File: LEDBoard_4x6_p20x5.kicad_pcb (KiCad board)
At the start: 2 copper layers, 0 parts

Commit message: fixed schematic ordering + placed parts
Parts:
- added C1: 10uF 6.3V, Capacitor_SMD:C_0603_1608Metric_Pad1.05x0.95mm_HandSolder, F.Cu at (75.2, 88.2)
- added C10: 100n, Capacitor_SMD:C_0603_1608Metric_Pad1.05x0.95mm_HandSolder, F.Cu at (122.2, 87.2)
- added C11: 10uF 6.3V, Capacitor_SMD:C_0603_1608Metric_Pad1.05x0.95mm_HandSolder, F.Cu at (115.2, 106.7)
- added C12: 100n, Capacitor_SMD:C_0603_1608Metric_Pad1.05x0.95mm_HandSolder, F.Cu at (122.2, 105.7)
- added C2: 100n, Capacitor_SMD:C_0603_1608Metric_Pad1.05x0.95mm_HandSolder, F.Cu at (82.2, 87.2)
- added C3: 10uF 6.3V, Capacitor_SMD:C_0603_1608Metric_Pad1.05x0.95mm_HandSolder, F.Cu at (75.2, 106.8)
- added C4: 100n, Capacitor_SMD:C_0603_1608Metric_Pad1.05x0.95mm_HandSolder, F.Cu at (82.2, 105.8)
- added C5: 10uF 6.3V, Capacitor_SMD:C_0603_1608Metric_Pad1.05x0.95mm_HandSolder, F.Cu at (115.2, 97.5)
- added C6: 100n, Capacitor_SMD:C_0603_1608Metric_Pad1.05x0.95mm_HandSolder, F.Cu at (122.2, 96.5)
- added C7: 10uF 6.3V, Capacitor_SMD:C_0603_1608Metric_Pad1.05x0.95mm_HandSolder, F.Cu at (75.2, 97.8)
- added C8: 100n, Capacitor_SMD:C_0603_1608Metric_Pad1.05x0.95mm_HandSolder, F.Cu at (82.2, 96.8)
- added C9: 10uF 6.3V, Capacitor_SMD:C_0603_1608Metric_Pad1.05x0.95mm_HandSolder, F.Cu at (115.2, 88.2)
- added D_0x0: LED_RGB, LEDs_SMD_NICHIA:LED_RGB_0706_1816Metric_ROHM_ThermalVias, F.Cu at (70.0, 87.5)
- added D_0x1: LED_RGB, LEDs_SMD_NICHIA:LED_RGB_0706_1816Metric_ROHM_ThermalVias, F.Cu at (70.0, 92.5)
- added D_0x2: LED_RGB, LEDs_SMD_NICHIA:LED_RGB_0706_1816Metric_ROHM_ThermalVias, F.Cu at (70.0, 97.5)
- added D_0x3: LED_RGB, LEDs_SMD_NICHIA:LED_RGB_0706_1816Metric_ROHM_ThermalVias, F.Cu at (70.0, 102.5)
- added D_0x4: LED_RGB, LEDs_SMD_NICHIA:LED_RGB_0706_1816Metric_ROHM_ThermalVias, F.Cu at (70.0, 107.5)
- added D_0x5: LED_RGB, LEDs_SMD_NICHIA:LED_RGB_0706_1816Metric_ROHM_ThermalVias, F.Cu at (70.0, 112.5)
- added D_1x0: LED_RGB, LEDs_SMD_NICHIA:LED_RGB_0706_1816Metric_ROHM_ThermalVias, F.Cu at (90.0, 87.5)
- added D_1x1: LED_RGB, LEDs_SMD_NICHIA:LED_RGB_0706_1816Metric_ROHM_ThermalVias, F.Cu at (90.0, 92.5)
- added D_1x2: LED_RGB, LEDs_SMD_NICHIA:LED_RGB_0706_1816Metric_ROHM_ThermalVias, F.Cu at (90.0, 97.5)
- added D_1x3: LED_RGB, LEDs_SMD_NICHIA:LED_RGB_0706_1816Metric_ROHM_ThermalVias, F.Cu at (90.0, 102.6)
- added D_1x4: LED_RGB, LEDs_SMD_NICHIA:LED_RGB_0706_1816Metric_ROHM_ThermalVias, F.Cu at (90.0, 107.5)
- added D_1x5: LED_RGB, LEDs_SMD_NICHIA:LED_RGB_0706_1816Metric_ROHM_ThermalVias, F.Cu at (90.0, 112.5)
- added D_2x0: LED_RGB, LEDs_SMD_NICHIA:LED_RGB_0706_1816Metric_ROHM_ThermalVias, F.Cu at (110.0, 87.5)
- added D_2x1: LED_RGB, LEDs_SMD_NICHIA:LED_RGB_0706_1816Metric_ROHM_ThermalVias, F.Cu at (110.0, 92.5)
- added D_2x2: LED_RGB, LEDs_SMD_NICHIA:LED_RGB_0706_1816Metric_ROHM_ThermalVias, F.Cu at (110.0, 97.5)
- added D_2x3: LED_RGB, LEDs_SMD_NICHIA:LED_RGB_0706_1816Metric_ROHM_ThermalVias, F.Cu at (110.0, 102.5)
- added D_2x4: LED_RGB, LEDs_SMD_NICHIA:LED_RGB_0706_1816Metric_ROHM_ThermalVias, F.Cu at (110.0, 107.5)
- added D_2x5: LED_RGB, LEDs_SMD_NICHIA:LED_RGB_0706_1816Metric_ROHM_ThermalVias, F.Cu at (110.0, 112.5)
- added D_3x0: LED_RGB, LEDs_SMD_NICHIA:LED_RGB_0706_1816Metric_ROHM_ThermalVias, F.Cu at (130.0, 87.5)
- added D_3x1: LED_RGB, LEDs_SMD_NICHIA:LED_RGB_0706_1816Metric_ROHM_ThermalVias, F.Cu at (130.0, 92.5)
- added D_3x2: LED_RGB, LEDs_SMD_NICHIA:LED_RGB_0706_1816Metric_ROHM_ThermalVias, F.Cu at (130.0, 97.5)
- added D_3x3: LED_RGB, LEDs_SMD_NICHIA:LED_RGB_0706_1816Metric_ROHM_ThermalVias, F.Cu at (130.0, 102.5)
- added D_3x4: LED_RGB, LEDs_SMD_NICHIA:LED_RGB_0706_1816Metric_ROHM_ThermalVias, F.Cu at (130.0, 107.5)
- added D_3x5: LED_RGB, LEDs_SMD_NICHIA:LED_RGB_0706_1816Metric_ROHM_ThermalVias, F.Cu at (130.0, 112.5)
- added H1: MH_M3, MountingHole:MountingHole_3.2mm_M3_ISO7380_Pad, F.Cu at (94.9, 95.0)
- added H2: MH_M3, MountingHole:MountingHole_3.2mm_M3_ISO7380_Pad, F.Cu at (105.0, 105.0)
- added J1: signal_in, Connector_PinHeader_2.54mm:PinHeader_1x04_P2.54mm_Vertical, F.Cu at (96.2, 88.5)
- added J2: signal_out, Connector_PinHeader_2.54mm:PinHeader_1x04_P2.54mm_Vertical, F.Cu at (96.2, 111.5)
- added J3: power_in, Connector_PinHeader_2.54mm:PinHeader_1x02_P2.54mm_Vertical, F.Cu at (96.2, 107.6)
- added J4: power_out, Connector_PinHeader_2.54mm:PinHeader_1x02_P2.54mm_Vertical, F.Cu at (101.3, 93.7)
- added R1: 2k7 0.1%, Resistor_SMD:R_0603_1608Metric_Pad1.05x0.95mm_HandSolder, F.Cu at (77.8, 87.2)
- added R2: 2k7 0.1%, Resistor_SMD:R_0603_1608Metric_Pad1.05x0.95mm_HandSolder, F.Cu at (77.8, 96.8)
- added R3: 2k7 0.1%, Resistor_SMD:R_0603_1608Metric_Pad1.05x0.95mm_HandSolder, F.Cu at (77.8, 105.8)
- added R4: 2k7 0.1%, Resistor_SMD:R_0603_1608Metric_Pad1.05x0.95mm_HandSolder, F.Cu at (117.8, 87.2)
- added R5: 2k7 0.1%, Resistor_SMD:R_0603_1608Metric_Pad1.05x0.95mm_HandSolder, F.Cu at (117.8, 96.5)
- added R6: 2k7 0.1%, Resistor_SMD:R_0603_1608Metric_Pad1.05x0.95mm_HandSolder, F.Cu at (117.8, 105.7)
- added U1: TLC5971PWP, Package_SO:HTSSOP-20-1EP_4.4x6.5mm_P0.65mm_EP3.4x6.5mm_Mask2.75x3.43mm_ThermalVias, F.Cu at (80.0, 91.5)
- added U2: TLC5971PWP, Package_SO:HTSSOP-20-1EP_4.4x6.5mm_P0.65mm_EP3.4x6.5mm_Mask2.75x3.43mm_ThermalVias, F.Cu at (80.0, 101.0)
- added U3: TLC5971PWP, Package_SO:HTSSOP-20-1EP_4.4x6.5mm_P0.65mm_EP3.4x6.5mm_Mask2.75x3.43mm_ThermalVias, F.Cu at (80.0, 110.0)
- added U4: TLC5971PWP, Package_SO:HTSSOP-20-1EP_4.4x6.5mm_P0.65mm_EP3.4x6.5mm_Mask2.75x3.43mm_ThermalVias, F.Cu at (120.0, 91.5)
- added U5: TLC5971PWP, Package_SO:HTSSOP-20-1EP_4.4x6.5mm_P0.65mm_EP3.4x6.5mm_Mask2.75x3.43mm_ThermalVias, F.Cu at (120.0, 101.0)
- added U6: TLC5971PWP, Package_SO:HTSSOP-20-1EP_4.4x6.5mm_P0.65mm_EP3.4x6.5mm_Mask2.75x3.43mm_ThermalVias, F.Cu at (120.0, 110.0)
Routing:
- added copper zone on B.Cu, net GND
- added copper zone on F.Cu, net VCC_LED
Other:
- board outline added: 64 x 28 mm

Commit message: pcb mostly done
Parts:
- moved C5 13.1 mm to (126.8, 103.8), turned to 180 degrees
- moved C9 13.1 mm to (126.8, 94.2), turned to 180 degrees
- moved C11 13.0 mm to (126.8, 112.8), turned to 180 degrees
- moved J1 9.00 mm to (96.2, 97.5)
- moved J2 9.00 mm to (96.2, 102.5)
- moved C3 6.56 mm to (73.2, 113.0), turned to 0 degrees
- moved C7 5.85 mm to (73.2, 103.2), turned to 0 degrees
- moved C1 5.43 mm to (73.2, 93.2), turned to 0 degrees
- moved H1 5.00 mm to (95.0, 90.0)
- moved H2 5.00 mm to (105.0, 110.0)
- moved C6 3.93 mm to (125.8, 98.2), turned to 0 degrees
- moved C10 3.82 mm to (125.8, 88.8), turned to 0 degrees
- moved C12 3.82 mm to (125.8, 107.2), turned to 0 degrees
- moved R5 3.82 mm to (114.2, 98.0), turned to 180 degrees
- moved R4 3.77 mm to (114.2, 88.4), turned to 180 degrees
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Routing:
- net VCC_LED: track 0.00 -> 494.7 mm
- net GND: track 0.00 -> 399.0 mm, vias 0 -> 29
- net VCC: track 0.00 -> 108.0 mm, vias 0 -> 12
- net /clock_3-4: track 0.00 -> 49.3 mm, vias 0 -> 4
- net /data_3-4: track 0.00 -> 48.6 mm, vias 0 -> 4
- net /data_out: track 0.00 -> 38.2 mm, vias 0 -> 1
- net /clock_out: track 0.00 -> 35.6 mm, vias 0 -> 1
- net /clock_in: track 0.00 -> 27.1 mm, vias 0 -> 2
- net /data_in: track 0.00 -> 22.9 mm, vias 0 -> 2
- net /clock_2-3: track 0.00 -> 21.6 mm, vias 0 -> 2
- net /data_2-3: track 0.00 -> 20.9 mm, vias 0 -> 2
- net /clock_4-5: track 0.00 -> 20.5 mm, vias 0 -> 2
- net /data_4-5: track 0.00 -> 20.2 mm, vias 0 -> 2
- net /clock_5-6: track 0.00 -> 19.8 mm, vias 0 -> 2
- net /data_5-6: track 0.00 -> 19.3 mm, vias 0 -> 2
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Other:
- board size 64 x 28 mm -> 64 x 29 mm
- net class Default: clearance 0.2 -> 0.15; trace_width 0.25 -> 0.15; via_dia 0.8 -> 0.6; via_drill 0.4 -> 0.3
- net class led added: clearance 0.2, trace_width 0.2, via_dia 0.6, via_drill 0.3
- net class power added: clearance 0.2, trace_width 0.25, via_dia 0.6, via_drill 0.3
- rule trace_clearance: 0.2 -> 0.15
- rule trace_min: 0.2 -> 0.1
- rule via_min_drill: 0.3 -> 0.2

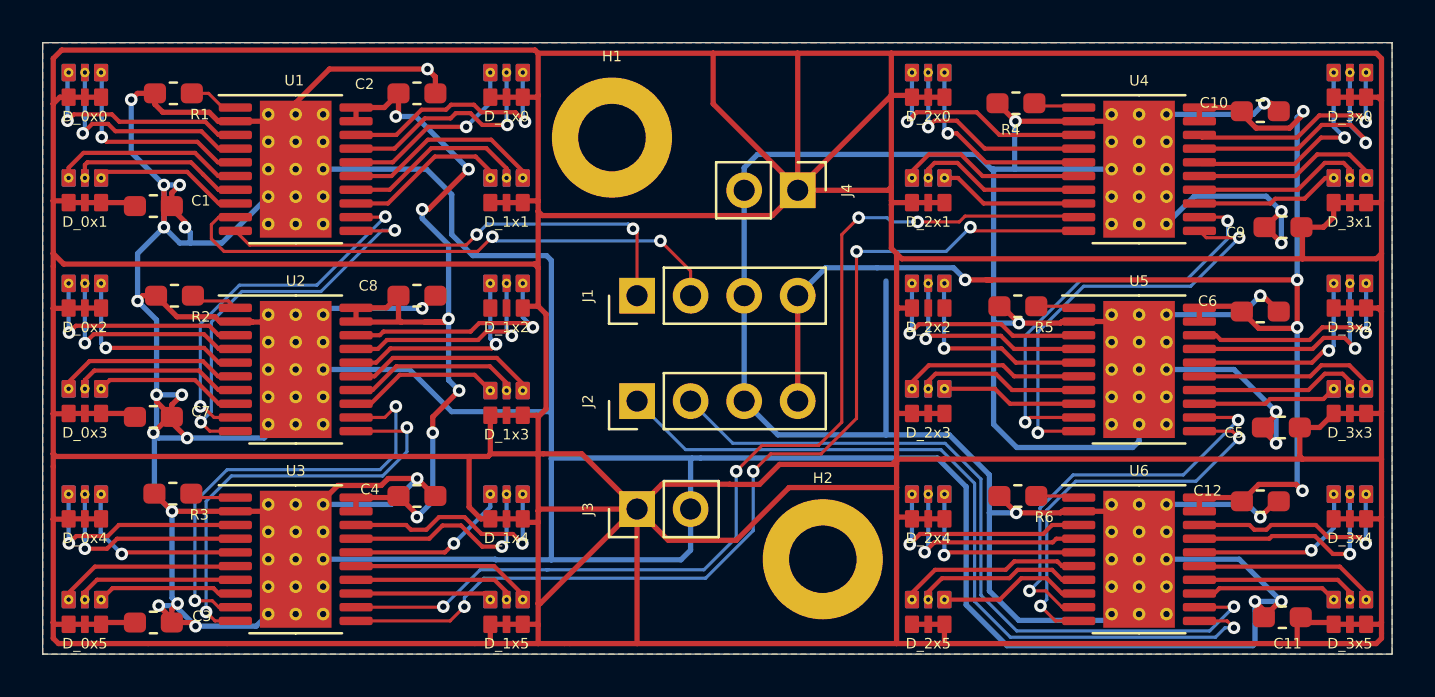
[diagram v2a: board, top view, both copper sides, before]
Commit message: added possible heatsink location
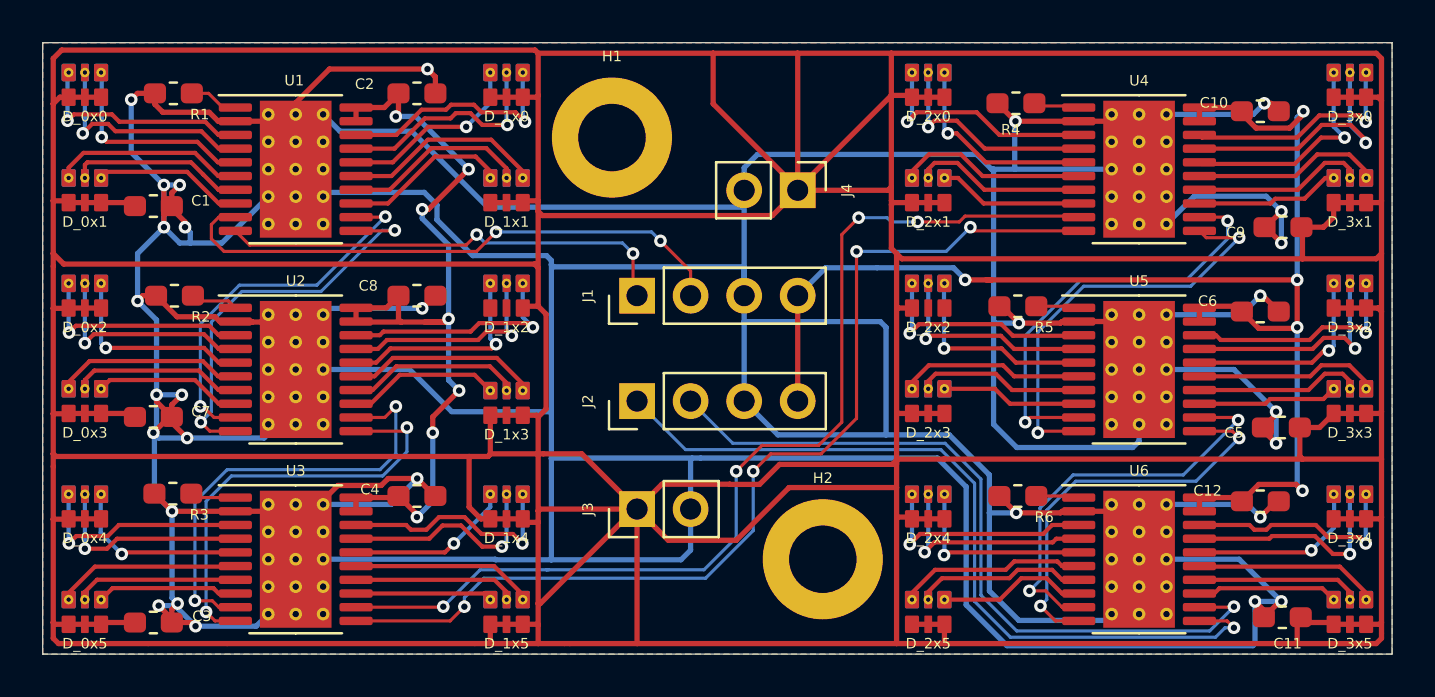
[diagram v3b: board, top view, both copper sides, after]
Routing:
- net GND: track 399.0 -> 436.0 mm
- net /data_in: track 22.9 -> 21.8 mm

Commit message: pcb done
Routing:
- net VCC: track 108.0 -> 131.6 mm, vias 12 -> 13
- net GND: track 436.0 -> 449.1 mm
- net /led_1x2_r: track 10.00 -> 9.31 mm
- net /led_1x2_b: track 11.0 -> 10.4 mm

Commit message: export done
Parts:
- moved R5 0.21 mm to (114.3, 98.2)
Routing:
- net VCC_LED: track 494.6 -> 555.3 mm
- net VCC: track 131.6 -> 128.2 mm
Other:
- board text added: "3.3V"
- board text added: "3.8-5.5V"
- board text added: "GND"
- board text added: "LEDBoard_4x6_p20x5 cc by Stefan Krüger s-light.eu 22.03.2020 v1.0.0"
- board text added: "VCC"
- board text added: "VCC: 3.3V logic: 3.3V VCC_LED: 3.8-5.5V"
- board text added: "VCC_LED"
- board text added: "clock"
- board text added: "data"
- board text added: "in"
- board text added: "out"
